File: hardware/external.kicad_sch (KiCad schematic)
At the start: 15 parts, among them J1 Conn_01x02, J11 Conn_01x02, J12 Conn_01x02

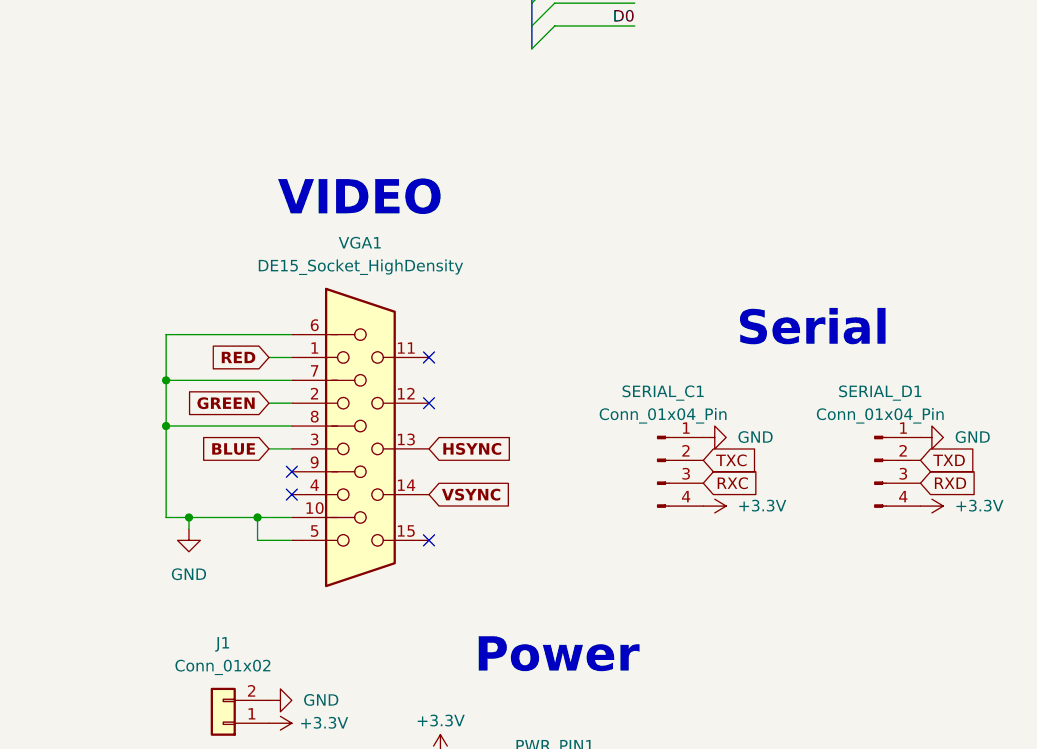
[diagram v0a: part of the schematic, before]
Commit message: Removed old VPU
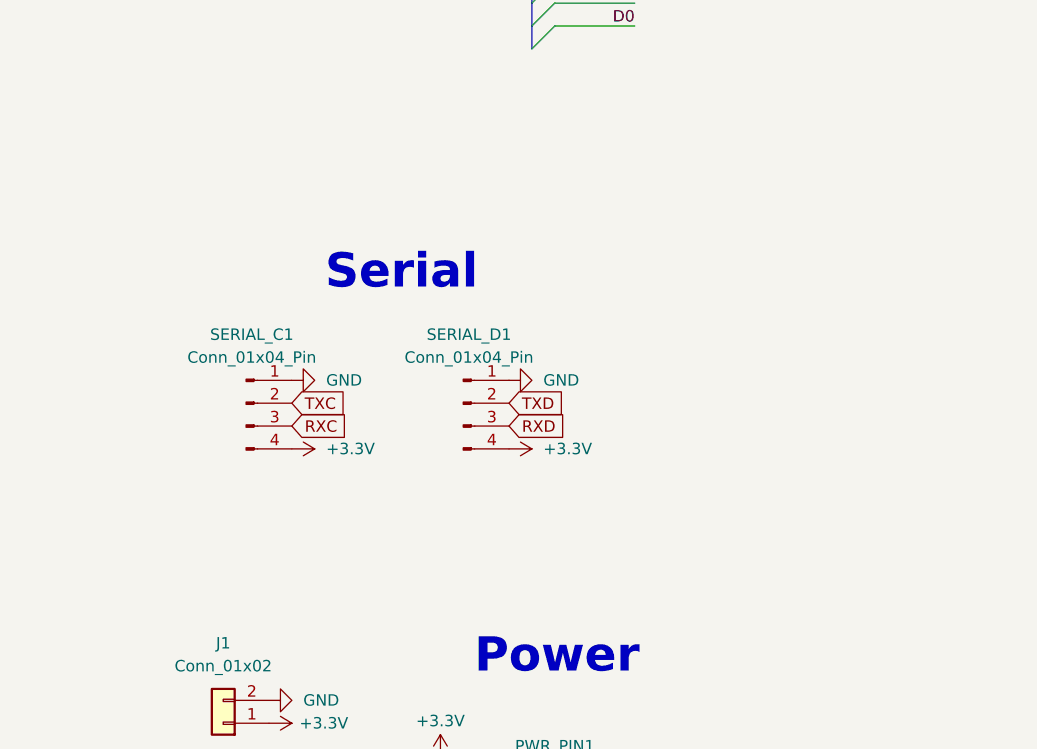
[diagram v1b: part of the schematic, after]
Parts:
- removed VGA1: DE15_Socket_HighDensity, Connector_Dsub:DSUB-15_Socket_Horizontal_P2.77x2.84mm_EdgePinOffset9.40mm, symbol Connector:DE15_Socket_HighDensity
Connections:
- no-connect marks 5 -> 0
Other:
- note removed: "VIDEO"
- moved on the sheet: SERIAL_C1, SERIAL_D1

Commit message: Removed old VPU
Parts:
- removed PortA_Ext1: Conn_01x10, Connector_PinHeader_2.54mm:PinHeader_1x10_P2.54mm_Vertical, symbol Connector_Generic:Conn_01x10
- removed SPI_EXT_{3}1, SPI_EXT_{3}2: Conn_02x07_Odd_Even, Connector_PinSocket_2.54mm:PinSocket_2x07_P2.54mm_Vertical, symbol Connector_Generic:Conn_02x07_Odd_Even
- added C30, C31: 1000µF, Fuse:Fuse_Bourns_MF-RG1000, symbol Device:C_Small
- added D1: SS14, Diode_SMD:D_SMA, symbol Diode:SS14
- added J3: Conn_01x07, Connector_PinHeader_2.54mm:PinHeader_1x07_P2.54mm_Vertical, symbol Connector_Generic:Conn_01x07
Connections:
- net +3.3V: now also J3.2 (Pin_2)
- net +5V: now also C31.1
- net AUDIO_{VDD}: now also C30.1, D1.1 (K); no longer J12.1 (Pin_1)
- net GND: now also C30.2, C31.2, J3.1 (Pin_1)
- net MISO: now also J3.4 (Pin_4)
- net MOSI: now also J3.5 (Pin_5)
- net SCK: now also J3.6 (Pin_6)
- net SPI_CS_{4}: now also J3.3 (Pin_3)
- net SPI_IRQ: now also J3.7 (Pin_7)
- new net: D1.2 (A), J12.1 (Pin_1)
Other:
- moved on the sheet: J1, J11, J12, PWR_PIN1, PortC_Ext1, PortD_Ext2
